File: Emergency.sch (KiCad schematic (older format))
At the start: 16 parts

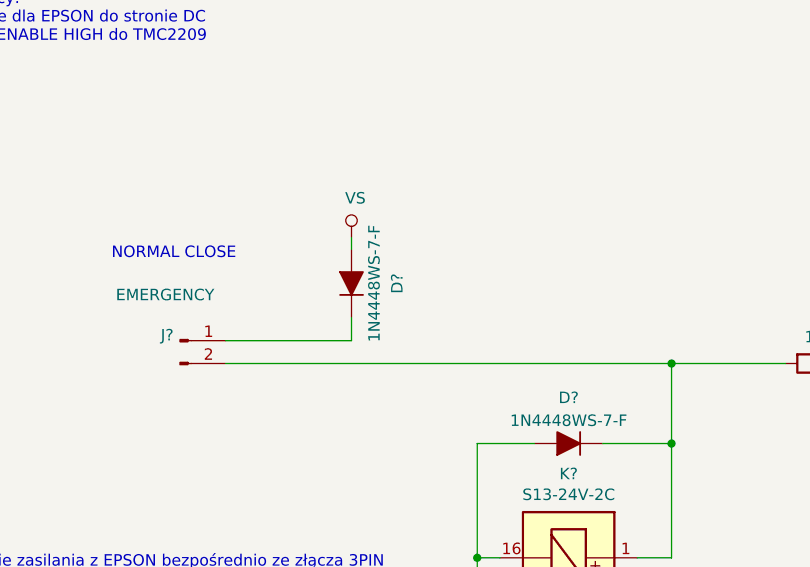
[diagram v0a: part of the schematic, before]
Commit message: Added Polyfuses and replace diodes
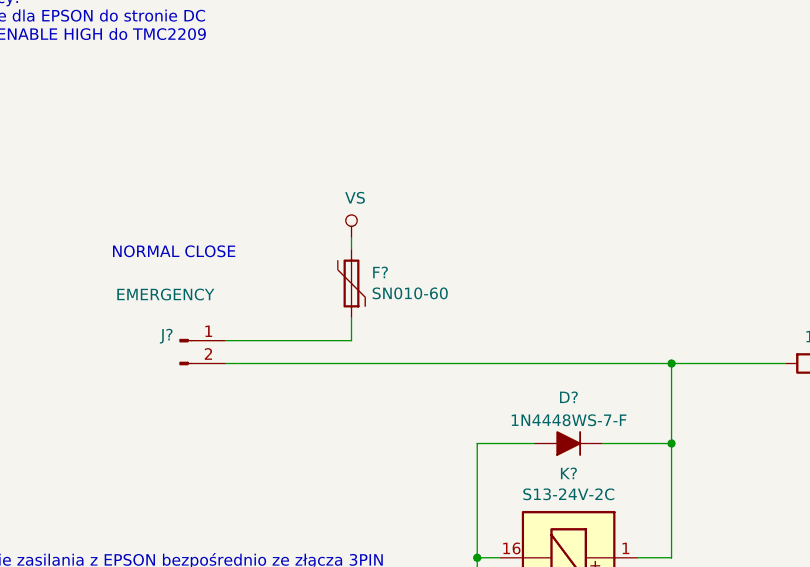
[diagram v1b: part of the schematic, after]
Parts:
- removed D?: 1N4448WS-7-F, Diode_SMD:D_SOD-323, symbol Device:D_ALT
- added F?: SN010-60, Fuse:Fuse_1206_3216Metric, symbol Device:Polyfuse
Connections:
- net VS: now also F?.2
- net at J?.1 (Pin_1): now also F?.1
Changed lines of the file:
@@
 $Descr A4 11693 8268
 encoding utf-8
-Sheet 8 9
+Sheet 8 10
 Title ""
 Date ""
@@
 Wire Wire Line
 	7500 3250 7500 3300
-$Comp
-L Device:D_ALT D?
-U 1 1 5E1664E5
+Wire Wire Line
+	3100 1800 3100 1850
+Wire Wire Line
+	3100 2250 3100 2150
+Wire Wire Line
+	2550 2250 3100 2250
+$Comp
+L Device:Polyfuse F?
+U 1 1 5E164594
 P 3100 2000
-AR Path="/5E1018C2/5E1664E5" Ref="D?"  Part="1"
-AR Path="/5E91D7CC/5E1664E5" Ref="D?"  Part="1"
-F 0 "D?" H 3100 1800 50  0000 C CNN
-F 1 "1N4448WS-7-F" H 3100 1900 50  0000 C CNN
-F 2 "Diode_SMD:D_SOD-323" H 3100 2000 50  0001 C CNN
+AR Path="/5E07245F/5E164594" Ref="F?"  Part="1"
+AR Path="/5E91D7CC/5E164594" Ref="F?"  Part="1"
+F 0 "F?" H 3012 1954 50  0000 R CNN
+F 1 "SN010-60 " H 3012 2045 50  0000 R CNN
+F 2 "Fuse:Fuse_1206_3216Metric" H 3150 1800 50  0001 L CNN
 F 3 "~" H 3100 2000 50  0001 C CNN
 	1    3100 2000
-	0    -1   -1   0
-$EndComp
-Wire Wire Line
-	3100 1800 3100 1850
-Wire Wire Line
-	3100 2250 3100 2150
-Wire Wire Line
-	2550 2250 3100 2250
+	-1   0    0    1
+$EndComp
 $EndSCHEMATC

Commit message: Improve schematics add new elements
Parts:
- added C?: 1nF, Capacitor_SMD:C_0603_1608Metric, symbol Device:C_Small
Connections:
- net EMERGENCY: now also C?.1
- net GND: now also C?.2
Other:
- moved on the sheet: R?, U?A, U?B
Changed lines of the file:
@@
 $EndComp
 Wire Wire Line
-	6650 2550 6650 2950
+	6650 2550 6650 2750
 $Comp
 L Device:R R?
@@
 Wire Wire Line
 	6150 2350 6350 2350
-Text GLabel 8050 2100 2    50   Output ~ 0
+Text GLabel 8250 2100 2    50   Output ~ 0
 EMERGENCY
 NoConn ~ 4350 3500
@@
 L Library:74HC2G32 U?
 U 1 1 5E1329B6
-P 8300 2850
-F 0 "U?" H 8450 3100 50  0000 C CNN
-F 1 "74HC2G32" H 8550 3000 50  0000 C CNN
-F 2 "Package_SO:VSSOP-8_2.3x2mm_P0.5mm" H 8300 2850 50  0001 C CNN
-F 3 "" H 8300 2850 50  0001 C CNN
-	1    8300 2850
+P 8450 3350
+F 0 "U?" H 8600 3600 50  0000 C CNN
+F 1 "74HC2G32" H 8700 3500 50  0000 C CNN
+F 2 "Package_SO:VSSOP-8_2.3x2mm_P0.5mm" H 8450 3350 50  0001 C CNN
+F 3 "" H 8450 3350 50  0001 C CNN
+	1    8450 3350
 	1    0    0    -1
 $EndComp
@@
 L Library:74HC2G32 U?
 U 2 1 5E133AA3
-P 8300 3600
-F 0 "U?" H 8275 3867 50  0000 C CNN
-F 1 "74HC2G32" H 8275 3776 50  0000 C CNN
-F 2 "Package_SO:VSSOP-8_2.3x2mm_P0.5mm" H 8300 3600 50  0001 C CNN
-F 3 "" H 8300 3600 50  0001 C CNN
-	2    8300 3600
+P 8450 4100
+F 0 "U?" H 8425 4367 50  0000 C CNN
+F 1 "74HC2G32" H 8425 4276 50  0000 C CNN
+F 2 "Package_SO:VSSOP-8_2.3x2mm_P0.5mm" H 8450 4100 50  0001 C CNN
+F 3 "" H 8450 4100 50  0001 C CNN
+	2    8450 4100
 	1    0    0    -1
 $EndComp
@@
 L power:GND #PWR?
 U 1 1 5E136188
-P 8300 3000
-F 0 "#PWR?" H 8300 2750 50  0001 C CNN
-F 1 "GND" H 8305 2827 50  0000 C CNN
-F 2 "" H 8300 3000 50  0001 C CNN
-F 3 "" H 8300 3000 50  0001 C CNN
-	1    8300 3000
+P 8450 3500
+F 0 "#PWR?" H 8450 3250 50  0001 C CNN
+F 1 "GND" H 8455 3327 50  0000 C CNN
+F 2 "" H 8450 3500 50  0001 C CNN
+F 3 "" H 8450 3500 50  0001 C CNN
+	1    8450 3500
 	1    0    0    -1
 $EndComp
@@
 L power:+3.3V #PWR?
 U 1 1 5E13670F
-P 8300 2500
-F 0 "#PWR?" H 8300 2350 50  0001 C CNN
-F 1 "+3.3V" H 8315 2673 50  0000 C CNN
-F 2 "" H 8300 2500 50  0001 C CNN
-F 3 "" H 8300 2500 50  0001 C CNN
-	1    8300 2500
-	1    0    0    -1
-$EndComp
-Wire Wire Line
-	8300 2500 8300 2750
-Wire Wire Line
-	8300 2950 8300 3000
-Wire Wire Line
-	8000 2800 7850 2800
-Wire Wire Line
-	7850 2800 7850 2100
-Connection ~ 7850 2100
-Wire Wire Line
-	7850 2100 8050 2100
-Wire Wire Line
-	7850 2800 7850 3550
-Wire Wire Line
-	7850 3550 8000 3550
-Connection ~ 7850 2800
-Text GLabel 8700 2850 2    50   Output ~ 0
+P 8450 3000
+F 0 "#PWR?" H 8450 2850 50  0001 C CNN
+F 1 "+3.3V" H 8465 3173 50  0000 C CNN
+F 2 "" H 8450 3000 50  0001 C CNN
+F 3 "" H 8450 3000 50  0001 C CNN
+	1    8450 3000
+	1    0    0    -1
+$EndComp
+Wire Wire Line
+	8450 3000 8450 3250
+Wire Wire Line
+	8450 3450 8450 3500
+Wire Wire Line
+	8150 3300 8000 3300
+Wire Wire Line
+	8000 3300 8000 4050
+Wire Wire Line
+	8000 4050 8150 4050
+Connection ~ 8000 3300
+Text GLabel 8850 3350 2    50   Output ~ 0
 Y_ENN
-Text GLabel 8700 3600 2    50   Output ~ 0
+Text GLabel 8850 4100 2    50   Output ~ 0
 Z_ENN
 Wire Wire Line
-	8550 2850 8700 2850
-Wire Wire Line
-	8550 3600 8700 3600
-Text GLabel 7300 2900 0    50   Input ~ 0
+	8700 3350 8850 3350
+Wire Wire Line
+	8700 4100 8850 4100
+Text GLabel 7450 3400 0    50   Input ~ 0
 Y_ENABLE
-Text GLabel 7300 3650 0    50   Input ~ 0
+Text GLabel 7450 4150 0    50   Input ~ 0
 Z_ENABLE
 Wire Wire Line
-	8000 2900 7500 2900
-Wire Wire Line
-	7300 3650 7500 3650
+	8150 3400 7650 3400
+Wire Wire Line
+	7450 4150 7650 4150
 $Comp
 L Device:R R?
 U 1 1 5E14A9EB
-P 7500 3450
-F 0 "R?" H 7570 3496 50  0000 L CNN
-F 1 "100kΩ" H 7570 3405 50  0000 L CNN
-F 2 "" V 7430 3450 50  0001 C CNN
-F 3 "~" H 7500 3450 50  0001 C CNN
-	1    7500 3450
+P 7650 3950
+F 0 "R?" H 7720 3996 50  0000 L CNN
+F 1 "100kΩ" H 7720 3905 50  0000 L CNN
+F 2 "" V 7580 3950 50  0001 C CNN
+F 3 "~" H 7650 3950 50  0001 C CNN
+	1    7650 3950
 	1    0    0    -1
 $EndComp
 Wire Wire Line
 	6650 2050 6650 2100
-Wire Wire Line
-	6650 2100 7850 2100
 Connection ~ 6650 2100
 Wire Wire Line
@@
 L Device:R R?
 U 1 1 5E14F006
-P 7500 2700
-F 0 "R?" H 7570 2746 50  0000 L CNN
-F 1 "100kΩ" H 7570 2655 50  0000 L CNN
-F 2 "" V 7430 2700 50  0001 C CNN
-F 3 "~" H 7500 2700 50  0001 C CNN
-	1    7500 2700
-	1    0    0    -1
-$EndComp
-Wire Wire Line
-	7500 3600 7500 3650
-Connection ~ 7500 3650
-Wire Wire Line
-	7500 3650 8000 3650
-Wire Wire Line
-	7500 2850 7500 2900
-Connection ~ 7500 2900
-Wire Wire Line
-	7500 2900 7300 2900
+P 7650 3200
+F 0 "R?" H 7720 3246 50  0000 L CNN
+F 1 "100kΩ" H 7720 3155 50  0000 L CNN
+F 2 "" V 7580 3200 50  0001 C CNN
+F 3 "~" H 7650 3200 50  0001 C CNN
+	1    7650 3200
+	1    0    0    -1
+$EndComp
+Wire Wire Line
+	7650 4100 7650 4150
+Connection ~ 7650 4150
+Wire Wire Line
+	7650 4150 8150 4150
+Wire Wire Line
+	7650 3350 7650 3400
+Connection ~ 7650 3400
+Wire Wire Line
+	7650 3400 7450 3400
 $Comp
 L power:+3.3V #PWR?
 U 1 1 5E151EAA
-P 7500 2500
-F 0 "#PWR?" H 7500 2350 50  0001 C CNN
-F 1 "+3.3V" H 7515 2673 50  0000 C CNN
-F 2 "" H 7500 2500 50  0001 C CNN
-F 3 "" H 7500 2500 50  0001 C CNN
-	1    7500 2500
+P 7650 3000
+F 0 "#PWR?" H 7650 2850 50  0001 C CNN
+F 1 "+3.3V" H 7665 3173 50  0000 C CNN
+F 2 "" H 7650 3000 50  0001 C CNN
+F 3 "" H 7650 3000 50  0001 C CNN
+	1    7650 3000
 	1    0    0    -1
 $EndComp
@@
 L power:+3.3V #PWR?
 U 1 1 5E152501
-P 7500 3250
-F 0 "#PWR?" H 7500 3100 50  0001 C CNN
-F 1 "+3.3V" H 7515 3423 50  0000 C CNN
-F 2 "" H 7500 3250 50  0001 C CNN
-F 3 "" H 7500 3250 50  0001 C CNN
-	1    7500 3250
-	1    0    0    -1
-$EndComp
-Wire Wire Line
-	7500 2500 7500 2550
-Wire Wire Line
-	7500 3250 7500 3300
+P 7650 3750
+F 0 "#PWR?" H 7650 3600 50  0001 C CNN
+F 1 "+3.3V" H 7665 3923 50  0000 C CNN
+F 2 "" H 7650 3750 50  0001 C CNN
+F 3 "" H 7650 3750 50  0001 C CNN
+	1    7650 3750
+	1    0    0    -1
+$EndComp
+Wire Wire Line
+	7650 3000 7650 3050
+Wire Wire Line
+	7650 3750 7650 3800
 Wire Wire Line
 	3100 1800 3100 1850
@@
 	-1   0    0    1
 $EndComp
+$Comp
+L Device:C_Small C?
+U 1 1 5E16709A
+P 7200 2350
+AR Path="/5DE588DC/5E16709A" Ref="C?"  Part="1"
+AR Path="/5E1018C2/5E16709A" Ref="C?"  Part="1"
+AR Path="/5E91D7CC/5E16709A" Ref="C?"  Part="1"
+F 0 "C?" H 7300 2400 50  0000 L CNN
+F 1 "1nF" H 7300 2300 50  0000 L CNN
+F 2 "Capacitor_SMD:C_0603_1608Metric" H 7200 2350 50  0001 C CNN
+F 3 "~" H 7200 2350 50  0001 C CNN
+	1    7200 2350
+	1    0    0    -1
+$EndComp
+Wire Wire Line
+	6650 2100 7200 2100
+Wire Wire Line
+	8000 2100 8000 3300
+Connection ~ 8000 2100
+Wire Wire Line
+	8000 2100 8250 2100
+Wire Wire Line
+	7200 2250 7200 2100
+Connection ~ 7200 2100
+Wire Wire Line
+	7200 2100 8000 2100
+Wire Wire Line
+	7200 2450 7200 2750
+Wire Wire Line
+	7200 2750 6650 2750
+Connection ~ 6650 2750
+Wire Wire Line
+	6650 2750 6650 2950
 $EndSCHEMATC

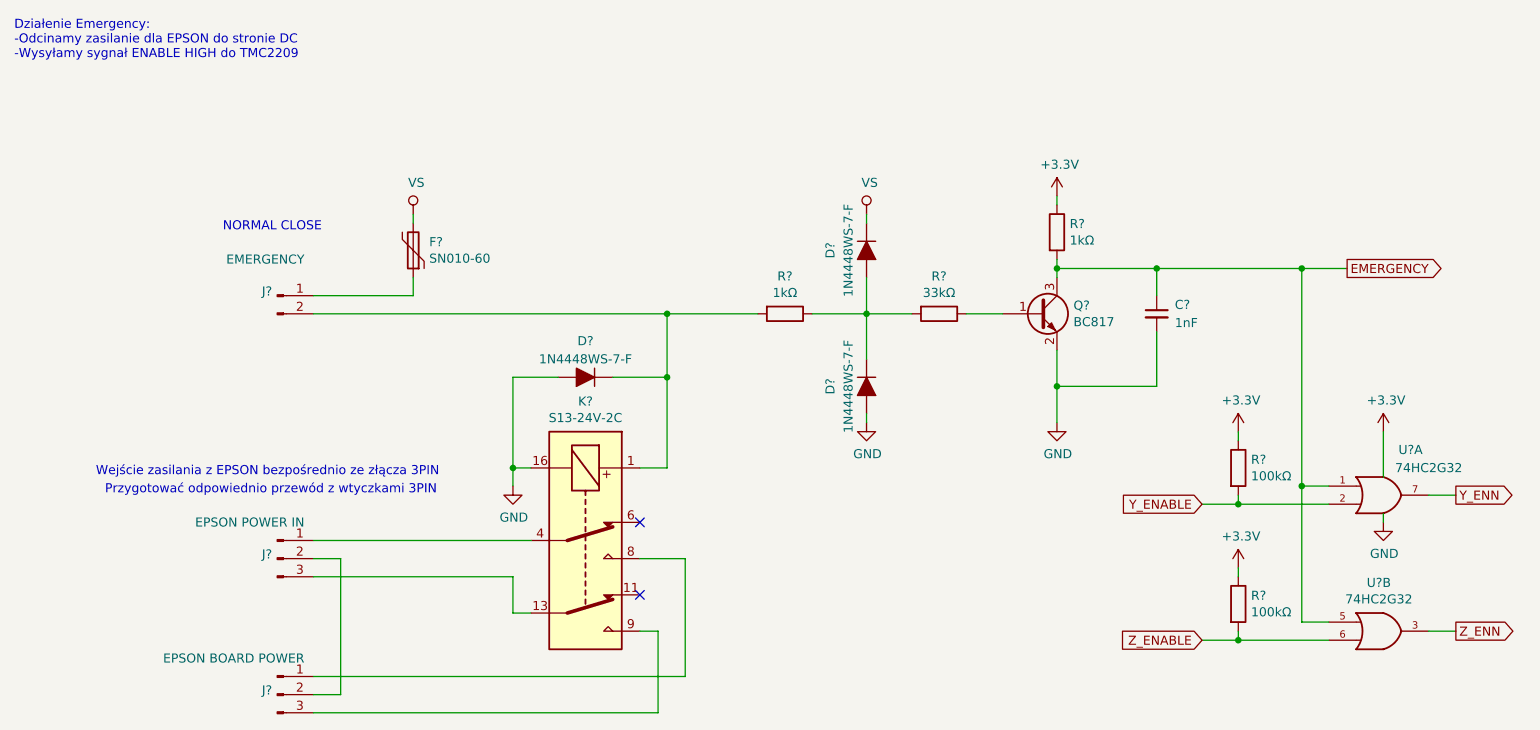
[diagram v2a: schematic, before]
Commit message: Numbering and finishing the schematic
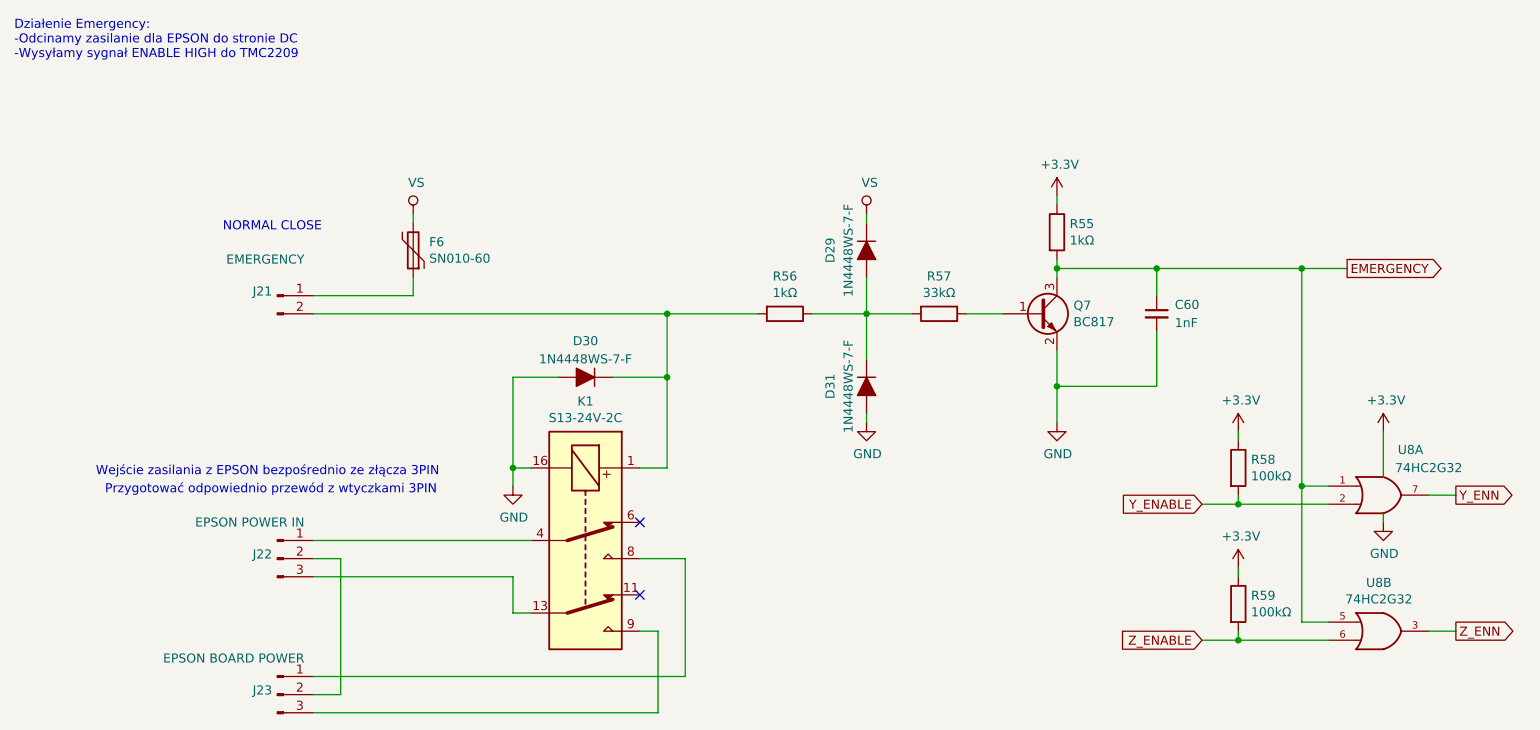
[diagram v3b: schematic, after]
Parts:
- gave numbers to parts that had none: 16
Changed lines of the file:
@@
 AR Path="/5E07245F/5E9227CA" Ref="J?"  Part="1"
 AR Path="/5E858220/5E9227CA" Ref="J?"  Part="1"
-AR Path="/5E91D7CC/5E9227CA" Ref="J?"  Part="1"
-F 0 "J?" H 2322 3724 50  0000 R CNN
+AR Path="/5E91D7CC/5E9227CA" Ref="J22"  Part="1"
+F 0 "J22" H 2322 3724 50  0000 R CNN
 F 1 "EPSON POWER IN" H 2500 3900 50  0000 R CNN
 F 2 "Connector_JST:JST_PH_B2B-PH-K_1x03_P2.00mm_Vertical" H 2350 3700 50  0001 C CNN
@@
 	2700 3700 2700 4450
 $Comp
-L Library:S13-24V-2C K?
+L Library:S13-24V-2C K1
 U 1 1 5E11641A
 P 4050 3600
-F 0 "K?" V 3283 3600 50  0000 C CNN
+F 0 "K1" V 3283 3600 50  0000 C CNN
 F 1 "S13-24V-2C" V 3374 3600 50  0000 C CNN
 F 2 "footprints:Relay_DPDT_Omron_G5V-2" H 4050 3600 50  0001 L CNN
@@
 AR Path="/5E07245F/5E922904" Ref="J?"  Part="1"
 AR Path="/5E858220/5E922904" Ref="J?"  Part="1"
-AR Path="/5E91D7CC/5E922904" Ref="J?"  Part="1"
-F 0 "J?" H 2322 4474 50  0000 R CNN
+AR Path="/5E91D7CC/5E922904" Ref="J23"  Part="1"
+F 0 "J23" H 2322 4474 50  0000 R CNN
 F 1 "EPSON BOARD POWER" H 2500 4650 50  0000 R CNN
 F 2 "Connector_JST:JST_PH_B2B-PH-K_1x03_P2.00mm_Vertical" H 2350 4450 50  0001 C CNN
@@
 AR Path="/5E07245F/5E1228A3" Ref="J?"  Part="1"
 AR Path="/5E858220/5E1228A3" Ref="J?"  Part="1"
-AR Path="/5E91D7CC/5E1228A3" Ref="J?"  Part="1"
-F 0 "J?" H 2322 2274 50  0000 R CNN
+AR Path="/5E91D7CC/5E1228A3" Ref="J21"  Part="1"
+F 0 "J21" H 2322 2274 50  0000 R CNN
 F 1 "EMERGENCY" H 2500 2450 50  0000 R CNN
 F 2 "Connector_JST:JST_PH_B2B-PH-K_1x02_P2.00mm_Vertical" H 2350 2250 50  0001 C CNN
@@
 P 3100 1800
 AR Path="/5E1018C2/5E127E8D" Ref="#PWR?"  Part="1"
-AR Path="/5E91D7CC/5E127E8D" Ref="#PWR?"  Part="1"
-F 0 "#PWR?" H 2900 1650 50  0001 C CNN
+AR Path="/5E91D7CC/5E127E8D" Ref="#PWR0140"  Part="1"
+F 0 "#PWR0140" H 2900 1650 50  0001 C CNN
 F 1 "VS" H 3117 1973 50  0000 C CNN
 F 2 "" H 3100 1800 50  0001 C CNN
@@
 	4500 3200 4350 3200
 $Comp
-L power:GND #PWR?
+L power:GND #PWR0146
 U 1 1 5E128738
 P 3650 3300
-F 0 "#PWR?" H 3650 3050 50  0001 C CNN
+F 0 "#PWR0146" H 3650 3050 50  0001 C CNN
 F 1 "GND" H 3655 3127 50  0000 C CNN
 F 2 "" H 3650 3300 50  0001 C CNN
@@
 P 4050 2700
 AR Path="/5E1018C2/5E12ABD3" Ref="D?"  Part="1"
-AR Path="/5E91D7CC/5E12ABD3" Ref="D?"  Part="1"
-F 0 "D?" H 4050 2500 50  0000 C CNN
+AR Path="/5E91D7CC/5E12ABD3" Ref="D30"  Part="1"
+F 0 "D30" H 4050 2500 50  0000 C CNN
 F 1 "1N4448WS-7-F" H 4050 2600 50  0000 C CNN
 F 2 "" H 4050 2700 50  0001 C CNN
@@
 Connection ~ 3650 3200
 $Comp
-L Device:R R?
+L Device:R R57
 U 1 1 5E137914
 P 6000 2350
-F 0 "R?" V 5793 2350 50  0000 C CNN
+F 0 "R57" V 5793 2350 50  0000 C CNN
 F 1 "33kΩ" V 5884 2350 50  0000 C CNN
 F 2 "" V 5930 2350 50  0001 C CNN
@@
 Connection ~ 4500 2350
 $Comp
-L Transistor_BJT:BC817 Q?
+L Transistor_BJT:BC817 Q7
 U 1 1 5E139012
 P 6550 2350
-F 0 "Q?" H 6741 2396 50  0000 L CNN
+F 0 "Q7" H 6741 2396 50  0000 L CNN
 F 1 "BC817" H 6741 2305 50  0000 L CNN
 F 2 "Package_TO_SOT_SMD:SOT-23" H 6750 2275 50  0001 L CIN
@@
 $EndComp
 $Comp
-L power:GND #PWR?
+L power:GND #PWR0143
 U 1 1 5E13A402
 P 6650 2950
-F 0 "#PWR?" H 6650 2700 50  0001 C CNN
+F 0 "#PWR0143" H 6650 2700 50  0001 C CNN
 F 1 "GND" H 6655 2777 50  0000 C CNN
 F 2 "" H 6650 2950 50  0001 C CNN
@@
 	6650 2550 6650 2750
 $Comp
-L Device:R R?
+L Device:R R55
 U 1 1 5E13AACA
 P 6650 1900
-F 0 "R?" H 6720 1946 50  0000 L CNN
+F 0 "R55" H 6720 1946 50  0000 L CNN
 F 1 "1kΩ" H 6720 1855 50  0000 L CNN
 F 2 "" V 6580 1900 50  0001 C CNN
@@
 P 5600 2000
 AR Path="/5E1018C2/5E121567" Ref="D?"  Part="1"
-AR Path="/5E91D7CC/5E121567" Ref="D?"  Part="1"
-F 0 "D?" H 5600 1800 50  0000 C CNN
+AR Path="/5E91D7CC/5E121567" Ref="D29"  Part="1"
+F 0 "D29" H 5600 1800 50  0000 C CNN
 F 1 "1N4448WS-7-F" H 5600 1900 50  0000 C CNN
 F 2 "Diode_SMD:D_SOD-323" H 5600 2000 50  0001 C CNN
@@
 P 5600 2750
 AR Path="/5E1018C2/5E121B31" Ref="D?"  Part="1"
-AR Path="/5E91D7CC/5E121B31" Ref="D?"  Part="1"
-F 0 "D?" H 5600 2550 50  0000 C CNN
+AR Path="/5E91D7CC/5E121B31" Ref="D31"  Part="1"
+F 0 "D31" H 5600 2550 50  0000 C CNN
 F 1 "1N4448WS-7-F" H 5600 2650 50  0000 C CNN
 F 2 "Diode_SMD:D_SOD-323" H 5600 2750 50  0001 C CNN
@@
 $EndComp
 $Comp
-L Device:R R?
+L Device:R R56
 U 1 1 5E122992
 P 5150 2350
-F 0 "R?" V 4943 2350 50  0000 C CNN
+F 0 "R56" V 4943 2350 50  0000 C CNN
 F 1 "1kΩ" V 5034 2350 50  0000 C CNN
 F 2 "" V 5080 2350 50  0001 C CNN
@@
 	5600 2600 5600 2350
 $Comp
-L power:GND #PWR?
+L power:GND #PWR0142
 U 1 1 5E12499E
 P 5600 2950
-F 0 "#PWR?" H 5600 2700 50  0001 C CNN
+F 0 "#PWR0142" H 5600 2700 50  0001 C CNN
 F 1 "GND" H 5605 2777 50  0000 C CNN
 F 2 "" H 5600 2950 50  0001 C CNN
@@
 P 5600 1800
 AR Path="/5E1018C2/5E1259C8" Ref="#PWR?"  Part="1"
-AR Path="/5E91D7CC/5E1259C8" Ref="#PWR?"  Part="1"
-F 0 "#PWR?" H 5400 1650 50  0001 C CNN
+AR Path="/5E91D7CC/5E1259C8" Ref="#PWR0141"  Part="1"
+F 0 "#PWR0141" H 5400 1650 50  0001 C CNN
 F 1 "VS" H 5617 1973 50  0000 C CNN
 F 2 "" H 5600 1800 50  0001 C CNN
@@
 	6650 1700 6650 1750
 $Comp
-L power:+3.3V #PWR?
+L power:+3.3V #PWR0139
 U 1 1 5E13B5C9
 P 6650 1700
-F 0 "#PWR?" H 6650 1550 50  0001 C CNN
+F 0 "#PWR0139" H 6650 1550 50  0001 C CNN
 F 1 "+3.3V" H 6665 1873 50  0000 C CNN
 F 2 "" H 6650 1700 50  0001 C CNN
@@
 $EndComp
 $Comp
-L Library:74HC2G32 U?
+L Library:74HC2G32 U8
 U 1 1 5E1329B6
 P 8450 3350
-F 0 "U?" H 8600 3600 50  0000 C CNN
+F 0 "U8" H 8600 3600 50  0000 C CNN
 F 1 "74HC2G32" H 8700 3500 50  0000 C CNN
 F 2 "Package_SO:VSSOP-8_2.3x2mm_P0.5mm" H 8450 3350 50  0001 C CNN
@@
 $EndComp
 $Comp
-L Library:74HC2G32 U?
+L Library:74HC2G32 U8
 U 2 1 5E133AA3
 P 8450 4100
-F 0 "U?" H 8425 4367 50  0000 C CNN
+F 0 "U8" H 8425 4367 50  0000 C CNN
 F 1 "74HC2G32" H 8425 4276 50  0000 C CNN
 F 2 "Package_SO:VSSOP-8_2.3x2mm_P0.5mm" H 8450 4100 50  0001 C CNN
@@
 $EndComp
 $Comp
-L power:GND #PWR?
+L power:GND #PWR0147
 U 1 1 5E136188
 P 8450 3500
-F 0 "#PWR?" H 8450 3250 50  0001 C CNN
+F 0 "#PWR0147" H 8450 3250 50  0001 C CNN
 F 1 "GND" H 8455 3327 50  0000 C CNN
 F 2 "" H 8450 3500 50  0001 C CNN
@@
 $EndComp
 $Comp
-L power:+3.3V #PWR?
+L power:+3.3V #PWR0145
 U 1 1 5E13670F
 P 8450 3000
-F 0 "#PWR?" H 8450 2850 50  0001 C CNN
+F 0 "#PWR0145" H 8450 2850 50  0001 C CNN
 F 1 "+3.3V" H 8465 3173 50  0000 C CNN
 F 2 "" H 8450 3000 50  0001 C CNN
@@
 	7450 4150 7650 4150
 $Comp
-L Device:R R?
+L Device:R R59
 U 1 1 5E14A9EB
 P 7650 3950
-F 0 "R?" H 7720 3996 50  0000 L CNN
+F 0 "R59" H 7720 3996 50  0000 L CNN
 F 1 "100kΩ" H 7720 3905 50  0000 L CNN
 F 2 "" V 7580 3950 50  0001 C CNN
@@
 	6650 2100 6650 2150
 $Comp
-L Device:R R?
+L Device:R R58
 U 1 1 5E14F006
 P 7650 3200
-F 0 "R?" H 7720 3246 50  0000 L CNN
+F 0 "R58" H 7720 3246 50  0000 L CNN
 F 1 "100kΩ" H 7720 3155 50  0000 L CNN
 F 2 "" V 7580 3200 50  0001 C CNN
@@
 	7650 3400 7450 3400
 $Comp
-L power:+3.3V #PWR?
+L power:+3.3V #PWR0144
 U 1 1 5E151EAA
 P 7650 3000
-F 0 "#PWR?" H 7650 2850 50  0001 C CNN
+F 0 "#PWR0144" H 7650 2850 50  0001 C CNN
 F 1 "+3.3V" H 7665 3173 50  0000 C CNN
 F 2 "" H 7650 3000 50  0001 C CNN
@@
 $EndComp
 $Comp
-L power:+3.3V #PWR?
+L power:+3.3V #PWR0148
 U 1 1 5E152501
 P 7650 3750
-F 0 "#PWR?" H 7650 3600 50  0001 C CNN
+F 0 "#PWR0148" H 7650 3600 50  0001 C CNN
 F 1 "+3.3V" H 7665 3923 50  0000 C CNN
 F 2 "" H 7650 3750 50  0001 C CNN
@@
 P 3100 2000
 AR Path="/5E07245F/5E164594" Ref="F?"  Part="1"
-AR Path="/5E91D7CC/5E164594" Ref="F?"  Part="1"
-F 0 "F?" H 3012 1954 50  0000 R CNN
+AR Path="/5E91D7CC/5E164594" Ref="F6"  Part="1"
+F 0 "F6" H 3012 1954 50  0000 R CNN
 F 1 "SN010-60 " H 3012 2045 50  0000 R CNN
 F 2 "Fuse:Fuse_1206_3216Metric" H 3150 1800 50  0001 L CNN
@@
 AR Path="/5DE588DC/5E16709A" Ref="C?"  Part="1"
 AR Path="/5E1018C2/5E16709A" Ref="C?"  Part="1"
-AR Path="/5E91D7CC/5E16709A" Ref="C?"  Part="1"
-F 0 "C?" H 7300 2400 50  0000 L CNN
+AR Path="/5E91D7CC/5E16709A" Ref="C60"  Part="1"
+F 0 "C60" H 7300 2400 50  0000 L CNN
 F 1 "1nF" H 7300 2300 50  0000 L CNN
 F 2 "Capacitor_SMD:C_0603_1608Metric" H 7200 2350 50  0001 C CNN
